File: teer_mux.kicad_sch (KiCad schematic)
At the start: 65 parts, among them IC1 MUX36S16IDWR, IC2 MUX36S16IDWR, J1 Conn_Triaxial, J10 855-22-016, J11 855-22-016, J12 855-22-016, J2 Conn_Triaxial, J3 Conn_Triaxial, J4 Conn_Triaxial, J5 HSTX, J6 855-22-016, J7 855-22-016, J8 855-22-016, J9 855-22-016, U1 5384, U10 MUX, U11 MUX, U12 MUX, U14 MUX, U15 MUX, U16 MUX, U17 MUX, U19 MUX, U2 SPLITRAIL_28, U20 MUX, U23 74LVC1GU04DRL, U24 CD74HC4514M96, U26 TMUX6112RTER, U3 ISO7760FDBQR, U4 ISO7762FDBQ, U5 OPA192, U6 OPA192, U7 OPA192, U8 OPA192, U9 MUX

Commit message: all nets routed
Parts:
- U2: footprint Package_DIP:SMDIP-28_W15.24mm -> Package_DIP:SMDIP-24_W15.24mm
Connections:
- net SW1 is gone; now on net SW: U4.3 (INB)
- net SW1_EN is gone; now on net SW_EN: U26.15 (SEL1), U4.14 (OUTB)
- net shorted_drains is gone; now on net shorted drains: U26.16 (D1)
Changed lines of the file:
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@@
 		)
 	)
-	(label "SW1_EN"
+	(label "SW_EN"
 		(at 138.43 87.63 180)
 		(effects
@@
 		)
 	)
-	(label "shorted_drains"
+	(label "shorted drains"
 		(at 177.8 148.59 0)
 		(effects
@@
 		)
 	)
-	(label "SW1"
+	(label "SW"
 		(at 102.87 87.63 0)
 		(effects
@@
 		)
 	)
-	(label "SW1_EN"
+	(label "SW_EN"
 		(at 177.8 151.13 0)
 		(effects
@@
 			)
 		)
-		(property "Footprint" "Package_DIP:SMDIP-28_W15.24mm"
+		(property "Footprint" "Package_DIP:SMDIP-24_W15.24mm"
 			(at 96.52 36.83 0)
 			(hide yes)

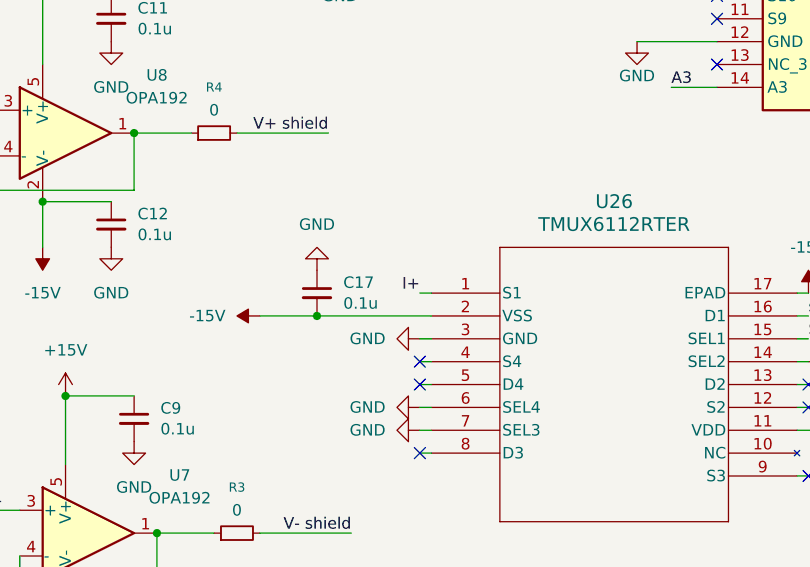
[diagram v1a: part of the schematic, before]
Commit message: fixed silkscreen
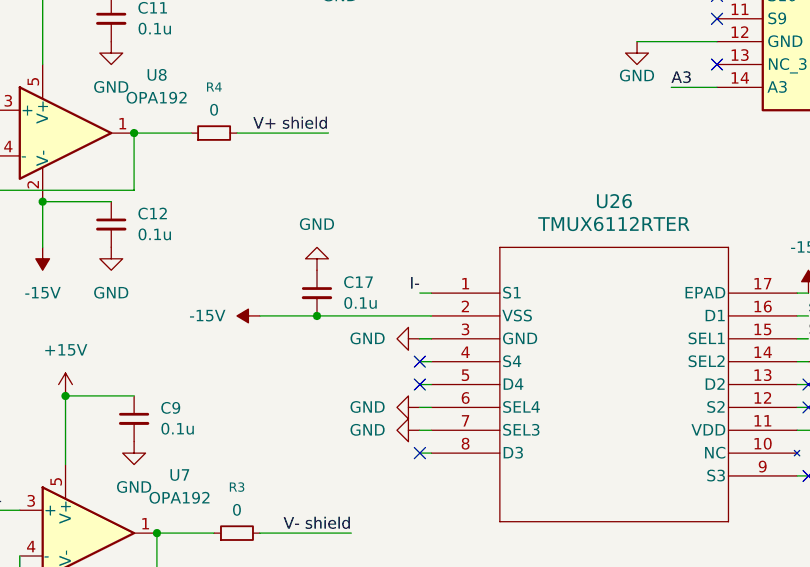
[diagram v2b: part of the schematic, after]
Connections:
- net I+: no longer U26.1 (S1)
- net I-: now also U26.1 (S1)
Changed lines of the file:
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@@
 		)
 	)
-	(label "I+"
+	(label "I-"
 		(at 134.62 146.05 180)
 		(effects

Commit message: made suggested edits, first production ver
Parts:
- added J13: V_diff, Connector_Triaxial_Custom:CBBJR79A, symbol Connector:Conn_Triaxial_Same_Side
- added JP1, JP2: Jumper, Jumper:SolderJumper-3_P1.3mm_Bridged12_Pad1.0x1.5mm, symbol Jumper:SolderJumper_3_Bridged12
- added S1: 2454985-2, 24549852, symbol 2454985-2:2454985-2
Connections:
- net EN_1: now also U14.21 (MUX_EN)
- net EN_10: no longer U20.21 (MUX_EN)
- net EN_2: now also U15.21 (MUX_EN)
- net EN_3: now also U16.21 (MUX_EN)
- net EN_4: now also U17.21 (MUX_EN)
- net EN_5: no longer U14.21 (MUX_EN)
- net EN_6: no longer U15.21 (MUX_EN)
- net EN_7: no longer U16.21 (MUX_EN)
- net EN_8: no longer U17.21 (MUX_EN)
- net EN_9: no longer U19.21 (MUX_EN)
- net GND: now also J13.3 (Ext); no longer U26.14 (SEL2)
- net I mux 1: now also IC1.19 (S1); no longer IC1.22 (S4)
- net I mux 2: now also IC1.20 (S2); no longer IC1.21 (S3)
- net I mux 3: now also IC1.21 (S3); no longer IC1.20 (S2)
- net I mux 4: now also IC1.22 (S4); no longer IC1.19 (S1)
- net I-: now also U26.12 (S2)
- net MUX_EN: now also U19.21 (MUX_EN), U20.21 (MUX_EN)
- net SW_EN: now also U26.14 (SEL2)
- net V+: now also JP1.2 (C); no longer J4.1 (In1)
- net V-: now also JP2.2 (C); no longer J3.1 (In1)
- net shorted V drains: now reaches U16.44 (SD)
- net shorted V drains: now also U14.44 (SD), U15.44 (SD), U17.44 (SD), U19.44 (SD), S1.A2 (2)
- net at U26.13 (D2): now also S1.A1 (1)
- net shorted drains renamed shorted I drains
- net shorted I drains: now also S1.B2 (4); no longer U26.16 (D1)
- new net: J13.1 (In1), JP1.1 (A)
- new net: J4.1 (In1), JP1.3 (B)
- new net: J3.1 (In1), JP2.3 (B)
- new net: S1.B1 (3), U26.16 (D1)
- new net: J13.2 (In2), JP2.1 (A)
- no-connect marks 96 -> 100
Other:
- moved on the sheet: J3, J4

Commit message: silkscreen fixes, minor edits
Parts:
- J1: value Conn_Triaxial -> I+
- J2: value Conn_Triaxial -> I-
- J3: value Conn_Triaxial -> V-
- J4: value Conn_Triaxial -> V+
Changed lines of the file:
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@@
 			)
 		)
-		(property "Value" "Conn_Triaxial"
+		(property "Value" "V-"
 			(at 75.2119 166.37 0)
 			(show_name no)
@@
 			)
 		)
-		(property "Value" "Conn_Triaxial"
+		(property "Value" "V+"
 			(at 72.6719 121.92 0)
 			(show_name no)
@@
 			)
 		)
-		(property "Value" "Conn_Triaxial"
+		(property "Value" "I-"
 			(at 20.6019 163.83 0)
 			(show_name no)
@@
 			)
 		)
-		(property "Value" "Conn_Triaxial"
+		(property "Value" "I+"
 			(at 20.6019 120.65 0)
 			(show_name no)

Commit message: shifted logic to correct indexing
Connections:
- net A0: no longer IC1.17 (A0), IC2.17 (A0), U24.2 (A0)
- net A1: now also IC1.17 (A0), IC2.17 (A0), U24.2 (A0); no longer IC1.16 (A1), IC2.16 (A1), U24.3 (A1)
- net A2: now also IC1.16 (A1), IC2.16 (A1), U24.3 (A1); no longer IC1.15 (A2), IC2.15 (A2), U24.21 (A2)
- net A3: now also IC1.15 (A2), IC2.15 (A2), U24.21 (A2); no longer IC1.14 (A3), IC2.14 (A3), U24.22 (A3)
- net I13: now also J7.14 (Pin_b14); no longer J7.15 (Pin_a16)
- net I14: no longer J7.16 (Pin_b16)
- net I27: now also J9.14 (Pin_b14); no longer J9.15 (Pin_a16)
- net I28: no longer J9.16 (Pin_b16)
- net I41: now also J11.14 (Pin_b14); no longer J11.15 (Pin_a16)
- net I42: no longer J11.16 (Pin_b16)
- net V14: no longer J7.14 (Pin_b14)
- net V28: no longer J9.14 (Pin_b14)
- net V42: no longer J11.14 (Pin_b14)
- net at JP1.1 (A): now also J4.1 (In1); no longer J13.1 (In1)
- net at JP1.3 (B): now also J13.1 (In1); no longer J4.1 (In1)
- net at J3.1 (In1): now also JP2.1 (A); no longer JP2.3 (B)
- net at J13.2 (In2): now also JP2.3 (B); no longer JP2.1 (A)
- no-connect marks 100 -> 101
